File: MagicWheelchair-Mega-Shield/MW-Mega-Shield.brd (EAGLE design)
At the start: 87.3 x 58.4 mm, 20 parts

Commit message: Update PCB, better PNGs
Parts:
- removed INPUT_1, INPUT_OPT: 736880-49, con-conrad:736880-49
- removed R3: 30kOhm, rcl:R0603
- removed TOUCH_DISABLE: (no value), jumper:JP1
- added R4: 30kOhm, rcl:R0603
- added S1: (no value), SparkFun-Retired:SWITCH_SPDT_SMD
- added X1, X2: TOBU3, con-hirschmann:TOBU3
- moved R1 16.3 mm to (52.1, 59.7)
- moved UNDER_VIN 14.0 mm to (57.1, 43.2)
- moved R2 10.9 mm to (30.5, 59.7)
- moved FIRE_DATA 10.2 mm to (49.5, 43.2)
- moved UNDER_GND 8.89 mm to (44.5, 43.2)
- moved FIRE_GND 5.08 mm to (35.6, 43.2)
- moved UNDER_DATA 3.81 mm to (30.5, 43.2)
- moved FIRE_VIN 2.54 mm to (25.4, 43.2)
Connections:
- removed net CS8: JP3.12
- new net CS2: JP3.6
- new net N$3: R4.1, S1.2
- net GND: now also S1.3, X1.2, X1.2@1, X1.2@2, X2.2, X2.2@1, X2.2@2; no longer R3.1
- net INPUT_1: now also X1.1; no longer INPUT_1.2
- net INPUT_OPT: now also JP3.12, X2.1; no longer INPUT_OPT.2, JP3.6
- net TOUCH_DISABLE: now also R4.2; no longer R3.2, TOUCH_DISABLE.2
- net VIN: now also S1.1; no longer TOUCH_DISABLE.1
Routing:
- net TOUCH_DISABLE: track 46.6 -> 26.9 mm
- net FIRE_DATA: track 5.50 -> 21.1 mm
- net N$3: track 0.00 -> 15.2 mm
- net INPUT_OPT: track 16.5 -> 4.34 mm
- net N$2: track 29.1 -> 17.3 mm
- net UNDER_DATA: track 5.50 -> 15.7 mm
- net N$1: track 24.9 -> 16.8 mm
- net VIN: track 97.6 -> 101.1 mm
- net INPUT_1: track 6.89 -> 4.34 mm
- net TOUCH_RESET: track 61.9 -> 64.0 mm
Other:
- board size 87.3 x 58.4 mm -> 87.3 x 59.7 mm

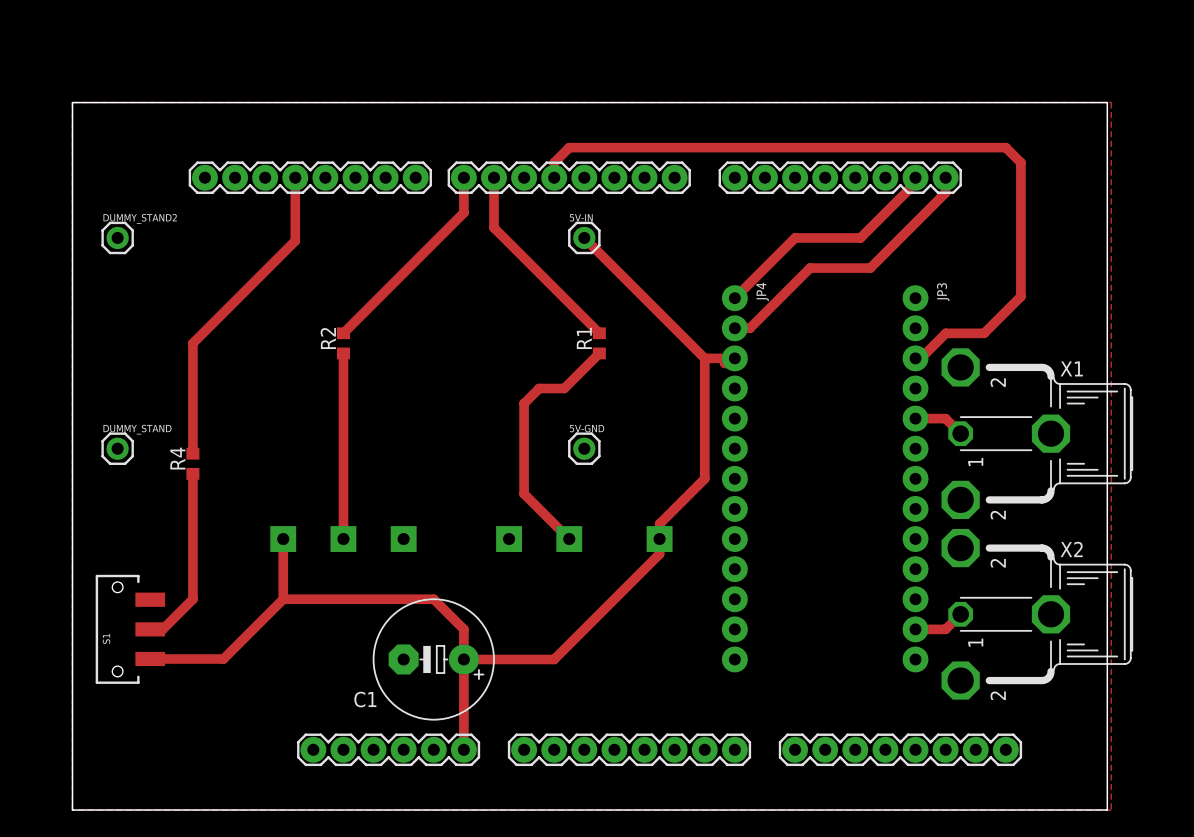
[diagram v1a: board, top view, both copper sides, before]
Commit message: Fix pad separation, switch holes, etc
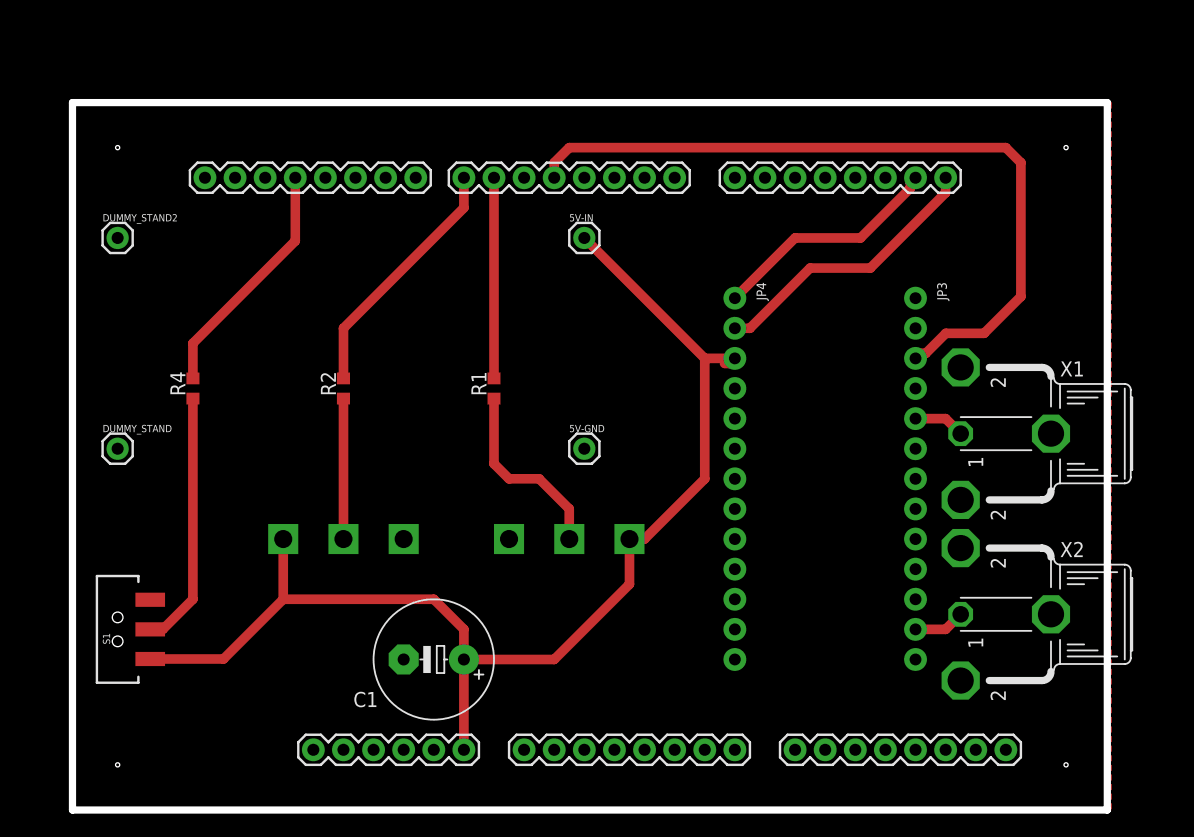
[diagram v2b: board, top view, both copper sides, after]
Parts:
- moved R1 9.67 mm to (43.2, 55.9)
- moved R4 6.35 mm to (17.8, 55.9)
- moved R2 3.81 mm to (30.5, 55.9)
- moved UNDER_VIN 2.54 mm to (54.6, 43.2)
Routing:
- net N$3: track 15.2 -> 21.6 mm
- net TOUCH_DISABLE: track 26.9 -> 20.5 mm
- net FIRE_DATA: track 21.1 -> 16.0 mm
- net UNDER_DATA: track 15.7 -> 11.9 mm
- net N$2: track 17.3 -> 21.1 mm
- net VIN: track 101.1 -> 101.8 mm
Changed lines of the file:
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@@
 <board>
 <plain>
-<wire x1="7.62" y1="20.32" x2="94.92" y2="20.32" width="0.127" layer="20"/>
-<wire x1="94.92" y1="20.32" x2="94.92" y2="80" width="0.127" layer="20"/>
-<wire x1="94.92" y1="80" x2="7.62" y2="80" width="0.127" layer="20"/>
-<wire x1="7.62" y1="80" x2="7.62" y2="20.32" width="0.127" layer="20"/>
+<wire x1="7.62" y1="20.32" x2="94.92" y2="20.32" width="0.6096" layer="20"/>
+<wire x1="94.92" y1="20.32" x2="94.92" y2="80" width="0.6096" layer="20"/>
+<wire x1="94.92" y1="80" x2="7.62" y2="80" width="0.6096" layer="20"/>
+<wire x1="7.62" y1="80" x2="7.62" y2="20.32" width="0.6096" layer="20"/>
+<hole x="11.43" y="76.2" drill="0.35"/>
+<hole x="11.43" y="24.13" drill="0.35"/>
+<hole x="91.44" y="24.13" drill="0.35"/>
+<hole x="91.44" y="76.2" drill="0.35"/>
 </plain>
 <attributes>
@@
 <elements>
 <element name="B1" library="SparkFun-Boards" package="ARDUINO_MEGA-SIMPLE_SHIELD" value="ARDUINO_MEGA_R3-SIMPLE" x="44.45" y="49.53"/>
-<element name="R1" library="rcl" library_urn="urn:adsk.eagle:library:334" package="R0603" package3d_urn="urn:adsk.eagle:package:23555/2" value="30kOhm" x="52.07" y="59.69" rot="R90">
-<attribute name="SPICEPREFIX" value="R" x="52.07" y="59.69" size="1.778" layer="27" rot="R90" display="off"/>
-</element>
-<element name="R2" library="rcl" library_urn="urn:adsk.eagle:library:334" package="R0603" package3d_urn="urn:adsk.eagle:package:23555/2" value="30kOhm" x="30.48" y="59.69" rot="R90">
-<attribute name="SPICEPREFIX" value="R" x="30.48" y="59.69" size="1.778" layer="27" rot="R90" display="off"/>
+<element name="R1" library="rcl" library_urn="urn:adsk.eagle:library:334" package="R0603" package3d_urn="urn:adsk.eagle:package:23555/2" value="30kOhm" x="43.18" y="55.88" rot="R90">
+<attribute name="SPICEPREFIX" value="R" x="43.18" y="55.88" size="1.778" layer="27" rot="R90" display="off"/>
+</element>
+<element name="R2" library="rcl" library_urn="urn:adsk.eagle:library:334" package="R0603" package3d_urn="urn:adsk.eagle:package:23555/2" value="30kOhm" x="30.48" y="55.88" rot="R90">
+<attribute name="SPICEPREFIX" value="R" x="30.48" y="55.88" size="1.778" layer="27" rot="R90" display="off"/>
 </element>
 <element name="C1" library="rcl" library_urn="urn:adsk.eagle:library:334" package="E5-10,5" package3d_urn="urn:adsk.eagle:package:23372/1" value="1000uF / 25V" x="38.1" y="33.02" rot="R180">
@@
 <element name="FIRE_DATA" library="dp_devices.v6" package="CON_PAD_SQUARE_1.02MM" value="PAD_TERMINAL-1.02MM_SQUARE" x="49.53" y="43.18"/>
 <element name="FIRE_GND" library="dp_devices.v6" package="CON_PAD_SQUARE_1.02MM" value="PAD_TERMINAL-1.02MM_SQUARE" x="35.56" y="43.18"/>
-<element name="UNDER_VIN" library="dp_devices.v6" package="CON_PAD_SQUARE_1.02MM" value="PAD_TERMINAL-1.02MM_SQUARE" x="57.15" y="43.18"/>
+<element name="UNDER_VIN" library="dp_devices.v6" package="CON_PAD_SQUARE_1.02MM" value="PAD_TERMINAL-1.02MM_SQUARE" x="54.61" y="43.18"/>
 <element name="UNDER_DATA" library="dp_devices.v6" package="CON_PAD_SQUARE_1.02MM" value="PAD_TERMINAL-1.02MM_SQUARE" x="30.48" y="43.18"/>
 <element name="UNDER_GND" library="dp_devices.v6" package="CON_PAD_SQUARE_1.02MM" value="PAD_TERMINAL-1.02MM_SQUARE" x="44.45" y="43.18"/>
@@
 <element name="DUMMY_STAND2" library="SparkFun-Connectors" package="1X01" value="" x="11.43" y="68.58"/>
 <element name="S1" library="SparkFun-Retired" package="SWITCH_SPDT_SMD" value="" x="11.43" y="35.56" rot="R90"/>
-<element name="R4" library="rcl" library_urn="urn:adsk.eagle:library:334" package="R0603" package3d_urn="urn:adsk.eagle:package:23555/2" value="30kOhm" x="17.78" y="49.53" rot="R90">
-<attribute name="SPICEPREFIX" value="R" x="17.78" y="49.53" size="1.778" layer="27" rot="R90" display="off"/>
+<element name="R4" library="rcl" library_urn="urn:adsk.eagle:library:334" package="R0603" package3d_urn="urn:adsk.eagle:package:23555/2" value="30kOhm" x="17.78" y="55.88" rot="R90">
+<attribute name="SPICEPREFIX" value="R" x="17.78" y="55.88" size="1.778" layer="27" rot="R90" display="off"/>
 </element>
 <element name="X1" library="con-hirschmann" library_urn="urn:adsk.eagle:library:153" package="TOBU3" package3d_urn="urn:adsk.eagle:package:7468/1" value="TOBU3" x="85.09" y="52.07" rot="R270">
@@
 <contactref element="B1" pad="7"/>
 <contactref element="R2" pad="2"/>
-<wire x1="30.48" y1="60.54" x2="40.64" y2="70.7" width="0.8128" layer="1"/>
-<wire x1="40.64" y1="70.7" x2="40.64" y2="73.66" width="0.8128" layer="1"/>
+<wire x1="30.48" y1="56.73" x2="30.48" y2="60.96" width="0.8128" layer="1"/>
+<wire x1="30.48" y1="60.96" x2="40.64" y2="71.12" width="0.8128" layer="1"/>
+<wire x1="40.64" y1="71.12" x2="40.64" y2="73.66" width="0.8128" layer="1"/>
 </signal>
 <signal name="N$1">
 <contactref element="B1" pad="6"/>
 <contactref element="R1" pad="2"/>
-<wire x1="52.07" y1="60.54" x2="43.18" y2="69.43" width="0.8128" layer="1"/>
-<wire x1="43.18" y1="69.43" x2="43.18" y2="73.66" width="0.8128" layer="1"/>
+<wire x1="43.18" y1="56.73" x2="43.18" y2="73.66" width="0.8128" layer="1"/>
 </signal>
 <signal name="GND">
@@
 <wire x1="62.62675" y1="57.9882" x2="63.0682" y2="57.9882" width="0.8128" layer="1"/>
 <wire x1="63.0682" y1="57.9882" x2="63.5" y2="58.42" width="0.8128" layer="1"/>
-<wire x1="40.64" y1="33.02" x2="48.26" y2="33.02" width="0.8128" layer="1"/>
-<wire x1="48.26" y1="33.02" x2="57.15" y2="41.91" width="0.8128" layer="1"/>
-<wire x1="57.15" y1="41.91" x2="57.15" y2="43.18" width="0.8128" layer="1"/>
+<wire x1="48.26" y1="33.02" x2="40.64" y2="33.02" width="0.8128" layer="1"/>
 <wire x1="14.18" y1="33.06" x2="20.36" y2="33.06" width="0.8128" layer="1"/>
 <wire x1="20.36" y1="33.06" x2="25.4" y2="38.1" width="0.8128" layer="1"/>
@@
 <wire x1="63.5" y1="58.42" x2="60.96" y2="58.42" width="0.8128" layer="1"/>
 <wire x1="60.96" y1="58.42" x2="50.8" y2="68.58" width="0.8128" layer="1"/>
-<wire x1="57.15" y1="43.18" x2="57.15" y2="44.45" width="0.8128" layer="1"/>
-<wire x1="60.96" y1="48.26" x2="60.96" y2="58.42" width="0.8128" layer="1"/>
-<wire x1="57.15" y1="44.45" x2="60.96" y2="48.26" width="0.8128" layer="1"/>
+<wire x1="60.96" y1="58.42" x2="60.96" y2="48.26" width="0.8128" layer="1"/>
+<wire x1="60.96" y1="48.26" x2="55.88" y2="43.18" width="0.8128" layer="1"/>
+<wire x1="55.88" y1="43.18" x2="54.61" y2="43.18" width="0.8128" layer="1"/>
+<wire x1="54.61" y1="43.18" x2="54.61" y2="39.37" width="0.8128" layer="1"/>
+<wire x1="54.61" y1="39.37" x2="48.26" y2="33.02" width="0.8128" layer="1"/>
 </signal>
 <signal name="FIRE_DATA">
 <contactref element="R1" pad="1"/>
 <contactref element="FIRE_DATA" pad="P"/>
-<wire x1="52.07" y1="58.84" x2="49.11" y2="55.88" width="0.8128" layer="1"/>
-<wire x1="49.11" y1="55.88" x2="46.99" y2="55.88" width="0.8128" layer="1"/>
-<wire x1="46.99" y1="55.88" x2="45.72" y2="54.61" width="0.8128" layer="1"/>
-<wire x1="45.72" y1="46.99" x2="49.53" y2="43.18" width="0.8128" layer="1"/>
-<wire x1="45.72" y1="54.61" x2="45.72" y2="46.99" width="0.8128" layer="1"/>
+<wire x1="43.18" y1="55.03" x2="43.18" y2="49.53" width="0.8128" layer="1"/>
+<wire x1="43.18" y1="49.53" x2="44.45" y2="48.26" width="0.8128" layer="1"/>
+<wire x1="44.45" y1="48.26" x2="46.99" y2="48.26" width="0.8128" layer="1"/>
+<wire x1="46.99" y1="48.26" x2="49.53" y2="45.72" width="0.8128" layer="1"/>
+<wire x1="49.53" y1="45.72" x2="49.53" y2="43.18" width="0.8128" layer="1"/>
 </signal>
 <signal name="UNDER_DATA">
 <contactref element="R2" pad="1"/>
 <contactref element="UNDER_DATA" pad="P"/>
-<wire x1="30.48" y1="43.18" x2="30.48" y2="58.84" width="0.8128" layer="1"/>
+<wire x1="30.48" y1="43.18" x2="30.48" y2="55.03" width="0.8128" layer="1"/>
 </signal>
 <signal name="TOUCH_DISABLE">
@@
 <contactref element="R4" pad="2"/>
 <wire x1="26.416" y1="73.66" x2="26.416" y2="68.326" width="0.8128" layer="1"/>
-<wire x1="17.78" y1="59.69" x2="17.78" y2="50.38" width="0.8128" layer="1"/>
+<wire x1="17.78" y1="59.69" x2="17.78" y2="56.73" width="0.8128" layer="1"/>
 <wire x1="26.416" y1="68.326" x2="17.78" y2="59.69" width="0.8128" layer="1"/>
 </signal>
@@
 <contactref element="S1" pad="2"/>
 <contactref element="R4" pad="1"/>
-<wire x1="17.78" y1="48.68" x2="17.78" y2="38.1" width="0.8128" layer="1"/>
+<wire x1="17.78" y1="55.03" x2="17.78" y2="38.1" width="0.8128" layer="1"/>
 <wire x1="17.78" y1="38.1" x2="15.24" y2="35.56" width="0.8128" layer="1"/>
 <wire x1="15.24" y1="35.56" x2="14.18" y2="35.56" width="0.8128" layer="1"/>

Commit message: Add master switch
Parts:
- added PWR_SW_IN, PWR_SW_OUT: PAD_TERMINAL-1.02MM_SQUARE, dp_devices.v6:CON_PAD_SQUARE_1.02MM
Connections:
- new net N$6: 5V-IN.1, PWR_SW_IN.P
- net VIN: now also PWR_SW_OUT.P; no longer 5V-IN.1
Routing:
- net VIN: track 101.8 -> 92.5 mm
- net N$6: track 0.00 -> 6.66 mm

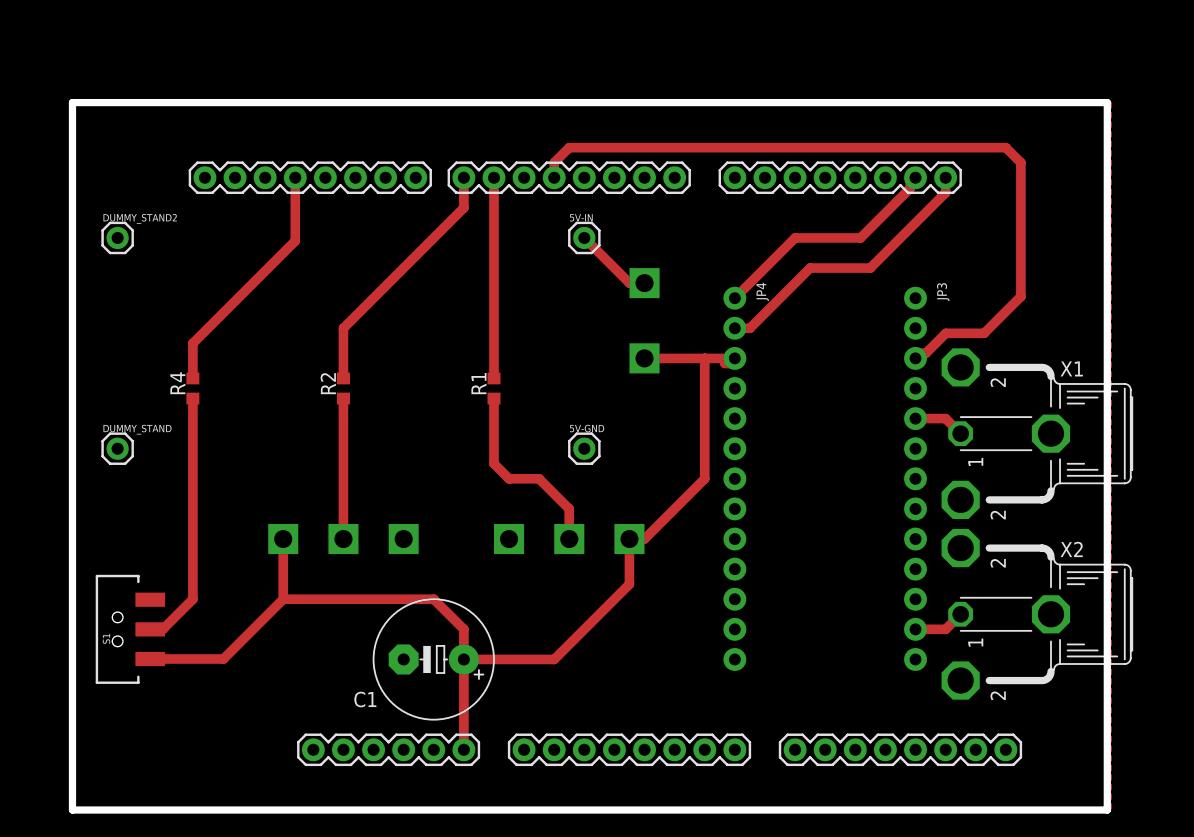
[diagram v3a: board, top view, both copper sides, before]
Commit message: Merge shields into one
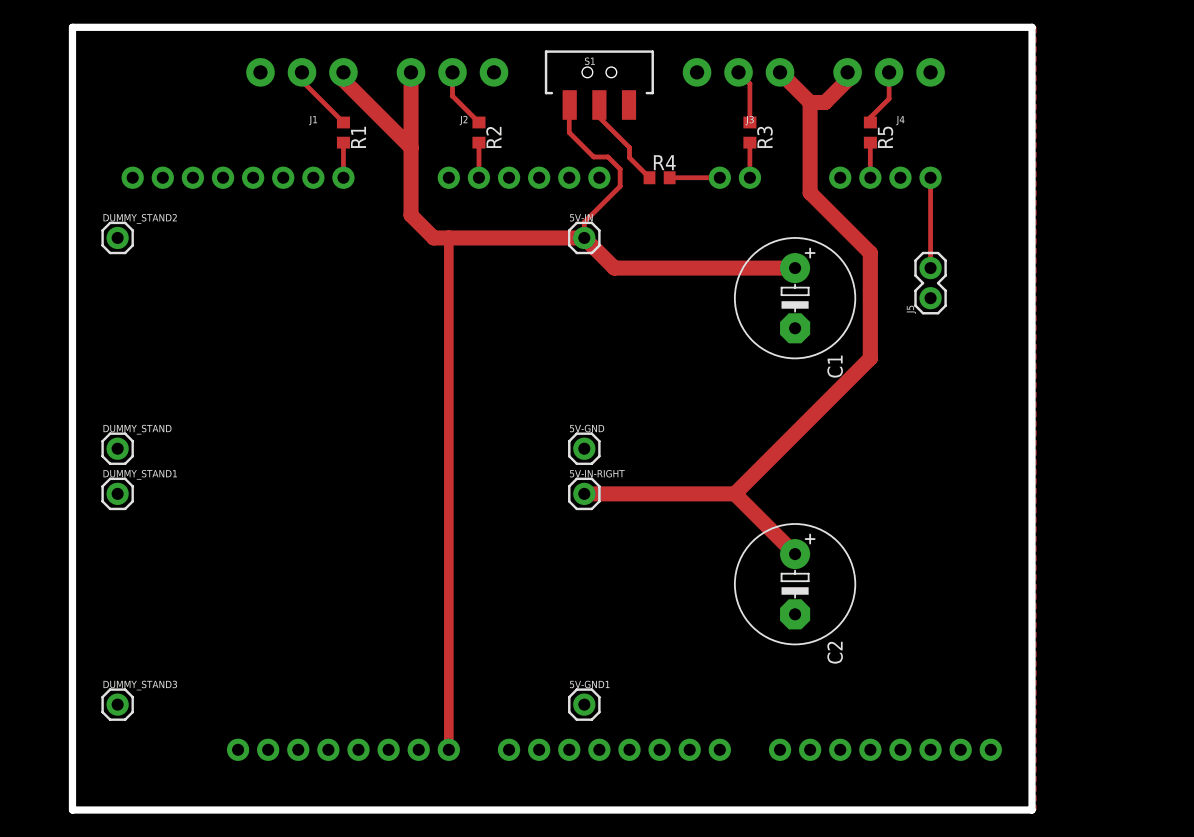
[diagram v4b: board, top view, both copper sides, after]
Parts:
- removed FIRE_DATA, FIRE_GND, FIRE_VIN, PWR_SW_IN, PWR_SW_OUT, UNDER_DATA, UNDER_GND, UNDER_VIN: PAD_TERMINAL-1.02MM_SQUARE, dp_devices.v6:CON_PAD_SQUARE_1.02MM
- removed JP3, JP4: (no value), microbuilder:1X13_ROUND_70
- removed X1, X2: TOBU3, con-hirschmann:TOBU3
- added 5V-GND1, 5V-IN-RIGHT, DUMMY_STAND1, DUMMY_STAND3: (no value), SparkFun-Connectors:1X01
- added C2: 1000uF / 25V, rcl:E5-10,5
- added J1, J2, J3, J4: (no value), SparkFun-Connectors:SCREWTERMINAL-3.5MM-3-NS
- added J5: (no value), SparkFun-Connectors:1X02
- added R3, R5: 470Ohm, rcl:R0603
- B1: value ARDUINO_MEGA_R3-SIMPLE -> ARDUINO_MEGA_R3FULL; device SparkFun-Boards:ARDUINO_MEGA-SIMPLE_SHIELD -> SparkFun-Boards:ARDUINO_MEGA_NO_SILK
- R1, R2: value 30kOhm -> 470Ohm
- moved S1 62.1 mm to (52.1, 82.5), turned to 0 degrees
- moved R4 43.2 mm to (57.1, 73.7), turned to 0 degrees
- moved C1 43.1 mm to (68.6, 63.5), turned to 270 degrees
- moved R1 25.0 mm to (30.5, 77.5), turned to 270 degrees
- moved R2 24.4 mm to (41.9, 77.5), turned to 270 degrees
- moved B1 1.27 mm to (43.2, 49.5)
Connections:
- removed net ADDR: JP3.13
- removed net CS: JP3.2
- removed net CS2: JP3.6
- removed net CS3: JP3.7
- removed net CS4: JP3.8
- removed net CS5: JP3.9
- removed net CS6: JP3.10
- removed net CS7: JP3.11
- removed net FIRE_DATA: FIRE_DATA.P, R1.1
- removed net INPUT_1: JP3.5, X1.1
- removed net INPUT_OPT: JP3.12, X2.1
- removed net IRQ: JP4.13
- removed net LED1: JP4.5
- removed net LED2: JP4.6
- removed net LED3: JP4.7
- removed net LED4: JP4.8
- removed net LED5: JP4.9
- removed net LED6: JP4.10
- removed net LED7: JP4.11
- removed net LED8: JP4.12
- removed net N$6: 5V-IN.1, PWR_SW_IN.P
- removed net SCL: B1.21, JP4.2
- removed net SDA: B1.20, JP4.1
- removed net TOUCH_RESET: B1.4, JP3.3
- removed net UNDER_DATA: R2.1, UNDER_DATA.P
- removed net WAKE/MOSI: JP3.1
- new net FIRE_LEFT_DATA: J1.2, R1.1
- new net FIRE_RIGHT_DATA: J3.2, R3.1
- new net N$5: B1.19, R5.2
- new net RIGHT_5V: 5V-IN-RIGHT.1, C2.+, J3.1, J4.3
- new net SWITCH: B1.21, J5.2
- new net UNDER_LEFT_DATA: J2.2, R2.1
- new net UNDER_RIGHT_DATA: J4.2, R5.1
- net GND: now also 5V-GND1.1, B1.GND, C2.-, J1.3, J2.1, J3.3, J4.1, J5.1; no longer B1.GND@0, FIRE_GND.P, JP4.4, UNDER_GND.P, X1.2, X1.2@1, X1.2@2, X2.2, X2.2@1, X2.2@2
- net N$1: now also B1.10; no longer B1.6
- net N$2: now also B1.6; no longer B1.7
- net N$4: now also B1.15, R3.2; no longer JP3.4
- net TOUCH_DISABLE: now also B1.14; no longer B1.12
- net VIN: now also 5V-IN.1, J1.1, J2.3; no longer FIRE_VIN.P, JP4.3, PWR_SW_OUT.P, UNDER_VIN.P
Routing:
- net RIGHT_5V: track 0.00 -> 67.9 mm
- net TOUCH_RESET: track 64.0 -> 0.00 mm
- net SCL: track 23.8 -> 0.00 mm
- net VIN: track 92.5 -> 113.2 mm
- net SDA: track 19.7 -> 0.00 mm
- net N$2: track 21.1 -> 2.96 mm
- net TOUCH_DISABLE: track 20.5 -> 4.23 mm
- net FIRE_DATA: track 16.0 -> 0.00 mm
- net N$1: track 16.9 -> 2.96 mm
- net N$3: track 21.6 -> 7.89 mm
- net UNDER_DATA: track 11.9 -> 0.00 mm
- net SWITCH: track 0.00 -> 7.62 mm
- net N$6: track 6.66 -> 0.00 mm
- net FIRE_LEFT_DATA: track 0.00 -> 5.68 mm
- net UNDER_LEFT_DATA: track 0.00 -> 5.15 mm
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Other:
- board size 87.3 x 59.7 mm -> 80.9 x 66 mm
